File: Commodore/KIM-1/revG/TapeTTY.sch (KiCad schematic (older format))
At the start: 45 parts, among them Q7 Q_NPN_CEB, U15 7400, U16 7404, U26 7438, U27 LM565, U28 LM311, U302 7438

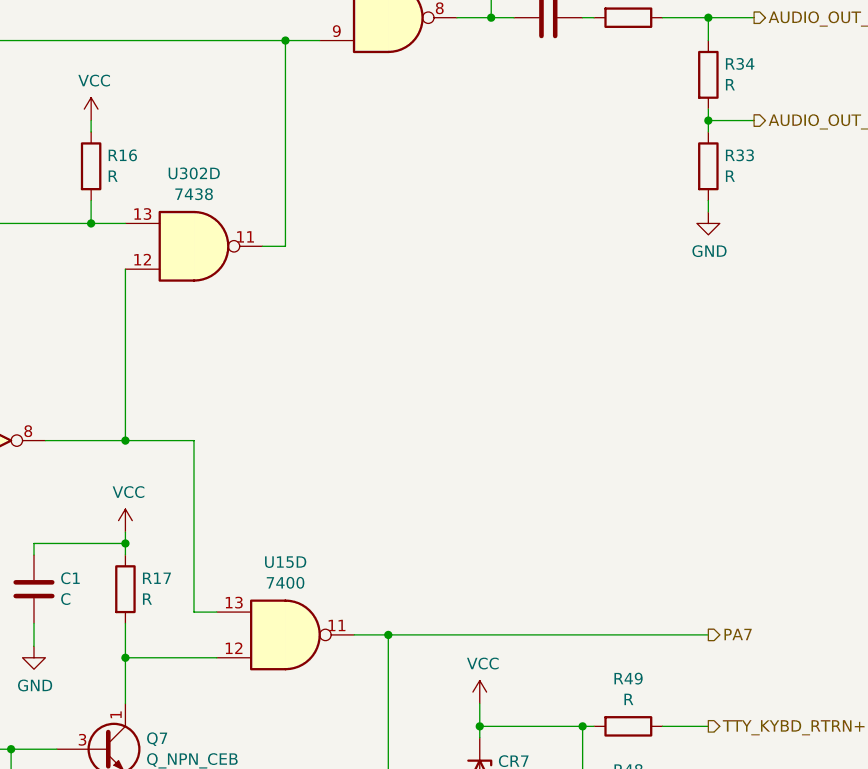
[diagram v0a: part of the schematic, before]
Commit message: Fixed missing/wrong designators, keypad labeling between sheets, PA & PB routing between sheets.
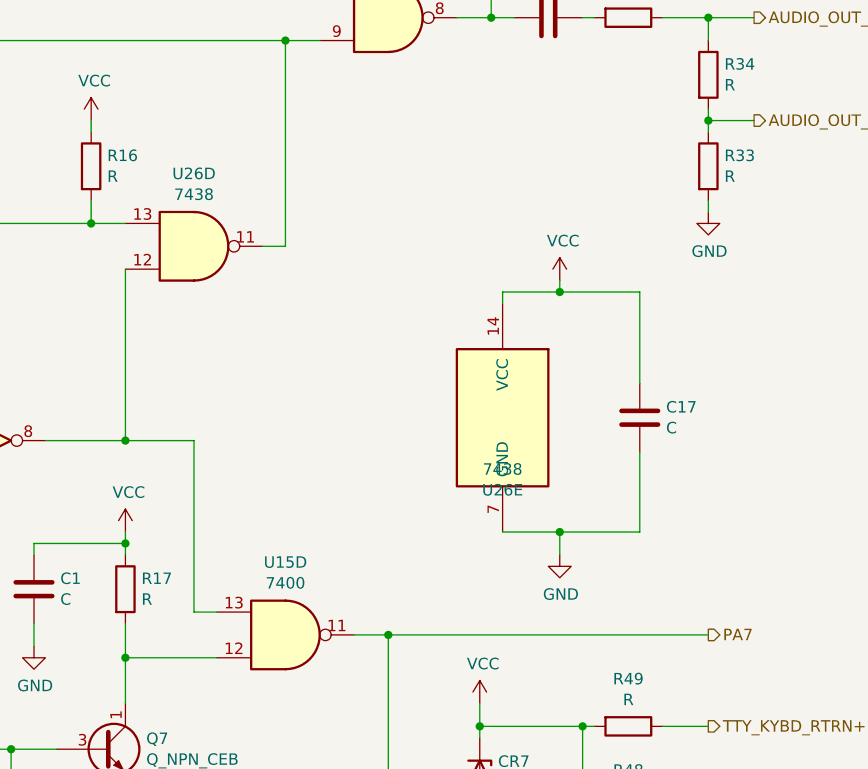
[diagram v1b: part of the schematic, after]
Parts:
- added C17: C, symbol Device:C
- added unit 5 of U26
- renumbered U302 to U26
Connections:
- net GND: now also C17.2, U26.7 (GND)
- net VCC: now also C17.1, U26.14 (VCC)
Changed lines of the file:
@@
 Connection ~ 9400 1500
 $Comp
-L 74xx_more:7438 U302
+L 74xx_more:7438 U26
 U 4 1 62491270
 P 8100 2500
-F 0 "U302" H 8100 2183 50  0000 C CNN
+F 0 "U26" H 8100 2183 50  0000 C CNN
 F 1 "7438" H 8100 2274 50  0000 C CNN
 F 2 "" H 8100 2500 50  0001 C CNN
@@
 Wire Wire Line
 	4500 4500 4500 4150
+$Comp
+L 74xx_more:7438 U26
+U 5 1 60E8022F
+P 9450 3250
+F 0 "U26" H 9450 2933 50  0000 C CNN
+F 1 "7438" H 9450 3024 50  0000 C CNN
+F 2 "" H 9450 3250 50  0001 C CNN
+F 3 "http://www.ti.com/lit/gpn/sn7438" H 9450 3250 50  0001 C CNN
+	5    9450 3250
+	-1   0    0    -1
+$EndComp
+$Comp
+L power:VCC #PWR0162
+U 1 1 60E94919
+P 9700 2650
+F 0 "#PWR0162" H 9700 2500 50  0001 C CNN
+F 1 "VCC" H 9715 2823 50  0000 C CNN
+F 2 "" H 9700 2650 50  0001 C CNN
+F 3 "" H 9700 2650 50  0001 C CNN
+	1    9700 2650
+	1    0    0    -1
+$EndComp
+$Comp
+L power:GND #PWR0163
+U 1 1 60E9528A
+P 9700 3850
+F 0 "#PWR0163" H 9700 3600 50  0001 C CNN
+F 1 "GND" H 9705 3677 50  0000 C CNN
+F 2 "" H 9700 3850 50  0001 C CNN
+F 3 "" H 9700 3850 50  0001 C CNN
+	1    9700 3850
+	1    0    0    -1
+$EndComp
+$Comp
+L Device:C C17
+U 1 1 60E959A3
+P 10050 3250
+F 0 "C17" H 10165 3296 50  0000 L CNN
+F 1 "C" H 10165 3205 50  0000 L CNN
+F 2 "" H 10088 3100 50  0001 C CNN
+F 3 "~" H 10050 3250 50  0001 C CNN
+	1    10050 3250
+	1    0    0    -1
+$EndComp
+Wire Wire Line
+	9450 2750 9450 2700
+Wire Wire Line
+	9450 2700 9700 2700
+Wire Wire Line
+	9700 2700 9700 2650
+Wire Wire Line
+	10050 3100 10050 2700
+Wire Wire Line
+	10050 2700 9700 2700
+Connection ~ 9700 2700
+Wire Wire Line
+	9450 3750 9700 3750
+Wire Wire Line
+	9700 3750 9700 3850
+Wire Wire Line
+	9700 3750 10050 3750
+Wire Wire Line
+	10050 3750 10050 3400
+Connection ~ 9700 3750
 $EndSCHEMATC

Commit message: Updated component values.
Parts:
- C1, C4: value C -> 1uF
- C10, C11, C9: value C -> 0.0068uF
- C12: value C -> 0.047uF
- C13: value C -> 0.022uF
- C14: value C -> 0.001uF
- C17, C7, C8: value C -> 0.1uF
- C5: value C -> 0.33uF
- C6: value C -> 0.22uF
- CR1, CR2, CR3, CR4: value D -> 1N914
- CR5, CR6: value D -> 1N4001
- CR7: value D_Zener -> 1N4735
- Q7: value Q_NPN_CEB -> 2N5371
- R10, R11, R8, R9: value R -> 10K
- R14, R15, R16, R17: value R -> 1K
- R33: value R -> 47
- R34, R50: value R -> 2.2K
- R40: value R -> 560
- R47: value R -> 220
- R48, R49: value R -> 150
- R51: value R -> 30K
- R52: value R -> 5M
- R6: value R -> 3.3K
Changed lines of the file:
@@
 P 10000 5000
 F 0 "R48" V 9793 5000 50  0000 C CNN
-F 1 "R" V 9884 5000 50  0000 C CNN
+F 1 "150" V 9884 5000 50  0000 C CNN
 F 2 "" V 9930 5000 50  0001 C CNN
 F 3 "~" H 10000 5000 50  0001 C CNN
@@
 P 7400 4000
 F 0 "C1" H 7515 4046 50  0000 L CNN
-F 1 "C" H 7515 3955 50  0000 L CNN
+F 1 "1uF" H 7515 3955 50  0000 L CNN
 F 2 "" H 7438 3850 50  0001 C CNN
 F 3 "~" H 7400 4000 50  0001 C CNN
@@
 P 9850 6000
 F 0 "CR6" V 9804 6080 50  0000 L CNN
-F 1 "D" V 9895 6080 50  0000 L CNN
+F 1 "1N4001" V 9895 6080 50  0000 L CNN
 F 2 "" H 9850 6000 50  0001 C CNN
 F 3 "~" H 9850 6000 50  0001 C CNN
@@
 P 9350 4800
 F 0 "CR7" V 9304 4880 50  0000 L CNN
-F 1 "D_Zener" V 9395 4880 50  0000 L CNN
+F 1 "1N4735" V 9395 4880 50  0000 L CNN
 F 2 "" H 9350 4800 50  0001 C CNN
 F 3 "~" H 9350 4800 50  0001 C CNN
@@
 P 7700 4700
 F 0 "Q7" H 7891 4746 50  0000 L CNN
-F 1 "Q_NPN_CEB" H 7891 4655 50  0000 L CNN
+F 1 "2N5371" H 7891 4655 50  0000 L CNN
 F 2 "" H 7900 4800 50  0001 C CNN
 F 3 "~" H 7700 4700 50  0001 C CNN
@@
 P 7800 4000
 F 0 "R17" H 7870 4046 50  0000 L CNN
-F 1 "R" H 7870 3955 50  0000 L CNN
+F 1 "1K" H 7870 3955 50  0000 L CNN
 F 2 "" V 7730 4000 50  0001 C CNN
 F 3 "~" H 7800 4000 50  0001 C CNN
@@
 P 7300 5000
 F 0 "R47" H 7370 5046 50  0000 L CNN
-F 1 "R" H 7370 4955 50  0000 L CNN
+F 1 "220" H 7370 4955 50  0000 L CNN
 F 2 "" V 7230 5000 50  0001 C CNN
 F 3 "~" H 7300 5000 50  0001 C CNN
@@
 P 6900 5000
 F 0 "C5" H 7015 5046 50  0000 L CNN
-F 1 "C" H 7015 4955 50  0000 L CNN
+F 1 "0.33uF" H 7015 4955 50  0000 L CNN
 F 2 "" H 6938 4850 50  0001 C CNN
 F 3 "~" H 6900 5000 50  0001 C CNN
@@
 P 6400 5000
 F 0 "CR5" V 6354 5080 50  0000 L CNN
-F 1 "D" V 6445 5080 50  0000 L CNN
+F 1 "1N4001" V 6445 5080 50  0000 L CNN
 F 2 "" H 6400 5000 50  0001 C CNN
 F 3 "~" H 6400 5000 50  0001 C CNN
@@
 P 10000 4600
 F 0 "R49" V 9793 4600 50  0000 C CNN
-F 1 "R" V 9884 4600 50  0000 C CNN
+F 1 "150" V 9884 4600 50  0000 C CNN
 F 2 "" V 9930 4600 50  0001 C CNN
 F 3 "~" H 10000 4600 50  0001 C CNN
@@
 P 10350 1750
 F 0 "R34" H 10420 1796 50  0000 L CNN
-F 1 "R" H 10420 1705 50  0000 L CNN
+F 1 "2.2K" H 10420 1705 50  0000 L CNN
 F 2 "" V 10280 1750 50  0001 C CNN
 F 3 "~" H 10350 1750 50  0001 C CNN
@@
 P 10350 2150
 F 0 "R33" H 10420 2196 50  0000 L CNN
-F 1 "R" H 10420 2105 50  0000 L CNN
+F 1 "47" H 10420 2105 50  0000 L CNN
 F 2 "" V 10280 2150 50  0001 C CNN
 F 3 "~" H 10350 2150 50  0001 C CNN
@@
 P 10000 1500
 F 0 "R6" V 9793 1500 50  0000 C CNN
-F 1 "R" V 9884 1500 50  0000 C CNN
+F 1 "3.3K" V 9884 1500 50  0000 C CNN
 F 2 "" V 9930 1500 50  0001 C CNN
 F 3 "~" H 10000 1500 50  0001 C CNN
@@
 P 9650 1500
 F 0 "C4" V 9398 1500 50  0000 C CNN
-F 1 "C" V 9489 1500 50  0000 C CNN
+F 1 "1uF" V 9489 1500 50  0000 C CNN
 F 2 "" H 9688 1350 50  0001 C CNN
 F 3 "~" H 9650 1500 50  0001 C CNN
@@
 P 9400 1150
 F 0 "R40" H 9470 1196 50  0000 L CNN
-F 1 "R" H 9470 1105 50  0000 L CNN
+F 1 "560" H 9470 1105 50  0000 L CNN
 F 2 "" V 9330 1150 50  0001 C CNN
 F 3 "~" H 9400 1150 50  0001 C CNN
@@
 P 7650 2150
 F 0 "R16" H 7720 2196 50  0000 L CNN
-F 1 "R" H 7720 2105 50  0000 L CNN
+F 1 "1K" H 7720 2105 50  0000 L CNN
 F 2 "" V 7580 2150 50  0001 C CNN
 F 3 "~" H 7650 2150 50  0001 C CNN
@@
 P 4900 1800
 F 0 "R52" V 4693 1800 50  0000 C CNN
-F 1 "R" V 4784 1800 50  0000 C CNN
+F 1 "5M" V 4784 1800 50  0000 C CNN
 F 2 "" V 4830 1800 50  0001 C CNN
 F 3 "~" H 4900 1800 50  0001 C CNN
@@
 P 4000 2250
 F 0 "C11" H 4115 2296 50  0000 L CNN
-F 1 "C" H 4115 2205 50  0000 L CNN
+F 1 "0.0068uF" H 4115 2205 50  0000 L CNN
 F 2 "" H 4038 2100 50  0001 C CNN
 F 3 "~" H 4000 2250 50  0001 C CNN
@@
 U 1 1 6253C63B
 P 3500 2500
-F 0 "R11" V 3293 2500 50  0000 C CNN
-F 1 "R" V 3384 2500 50  0000 C CNN
+F 0 "R11" V 3700 2500 50  0000 C CNN
+F 1 "10K" V 3600 2500 50  0000 C CNN
 F 2 "" V 3430 2500 50  0001 C CNN
 F 3 "~" H 3500 2500 50  0001 C CNN
@@
 P 3150 2250
 F 0 "C10" H 3265 2296 50  0000 L CNN
-F 1 "C" H 3265 2205 50  0000 L CNN
+F 1 "0.0068uF" H 3265 2205 50  0000 L CNN
 F 2 "" H 3188 2100 50  0001 C CNN
 F 3 "~" H 3150 2250 50  0001 C CNN
@@
 U 1 1 6253D3D7
 P 2800 2500
-F 0 "R10" V 2593 2500 50  0000 C CNN
-F 1 "R" V 2684 2500 50  0000 C CNN
+F 0 "R10" V 3000 2500 50  0000 C CNN
+F 1 "10K" V 2900 2500 50  0000 C CNN
 F 2 "" V 2730 2500 50  0001 C CNN
 F 3 "~" H 2800 2500 50  0001 C CNN
@@
 P 2450 2250
 F 0 "C9" H 2565 2296 50  0000 L CNN
-F 1 "C" H 2565 2205 50  0000 L CNN
+F 1 "0.0068uF" H 2565 2205 50  0000 L CNN
 F 2 "" H 2488 2100 50  0001 C CNN
 F 3 "~" H 2450 2250 50  0001 C CNN
@@
 U 1 1 625467C7
 P 2100 2500
-F 0 "R9" V 1893 2500 50  0000 C CNN
-F 1 "R" V 1984 2500 50  0000 C CNN
+F 0 "R9" V 2300 2500 50  0000 C CNN
+F 1 "10K" V 2200 2500 50  0000 C CNN
 F 2 "" V 2030 2500 50  0001 C CNN
 F 3 "~" H 2100 2500 50  0001 C CNN
@@
 P 1750 2250
 F 0 "C12" H 1865 2296 50  0000 L CNN
-F 1 "C" H 1865 2205 50  0000 L CNN
+F 1 "0.047uF" H 1865 2205 50  0000 L CNN
 F 2 "" H 1788 2100 50  0001 C CNN
 F 3 "~" H 1750 2250 50  0001 C CNN
@@
 P 1300 2250
 F 0 "C8" H 1415 2296 50  0000 L CNN
-F 1 "C" H 1415 2205 50  0000 L CNN
+F 1 "0.1uF" H 1415 2205 50  0000 L CNN
 F 2 "" H 1338 2100 50  0001 C CNN
 F 3 "~" H 1300 2250 50  0001 C CNN
@@
 P 1450 5350
 F 0 "C6" V 1198 5350 50  0000 C CNN
-F 1 "C" V 1289 5350 50  0000 C CNN
+F 1 "0.22uF" V 1289 5350 50  0000 C CNN
 F 2 "" H 1488 5200 50  0001 C CNN
 F 3 "~" H 1450 5350 50  0001 C CNN
@@
 P 2600 5000
 F 0 "CR1" V 2554 5080 50  0000 L CNN
-F 1 "D" V 2645 5080 50  0000 L CNN
+F 1 "1N914" V 2645 5080 50  0000 L CNN
 F 2 "" H 2600 5000 50  0001 C CNN
 F 3 "~" H 2600 5000 50  0001 C CNN
@@
 P 2950 5000
 F 0 "CR2" V 2996 4920 50  0000 R CNN
-F 1 "D" V 2905 4920 50  0000 R CNN
+F 1 "1N914" V 2905 4920 50  0000 R CNN
 F 2 "" H 2950 5000 50  0001 C CNN
 F 3 "~" H 2950 5000 50  0001 C CNN
@@
 P 3300 5000
 F 0 "R15" H 3230 4954 50  0000 R CNN
-F 1 "R" H 3230 5045 50  0000 R CNN
+F 1 "1K" H 3230 5045 50  0000 R CNN
 F 2 "" V 3230 5000 50  0001 C CNN
 F 3 "~" H 3300 5000 50  0001 C CNN
@@
 P 2000 5350
 F 0 "R8" V 1793 5350 50  0000 C CNN
-F 1 "R" V 1884 5350 50  0000 C CNN
+F 1 "10K" V 1884 5350 50  0000 C CNN
 F 2 "" V 1930 5350 50  0001 C CNN
 F 3 "~" H 2000 5350 50  0001 C CNN
@@
 P 2200 5000
 F 0 "R14" H 2130 4954 50  0000 R CNN
-F 1 "R" H 2130 5045 50  0000 R CNN
+F 1 "1K" H 2130 5045 50  0000 R CNN
 F 2 "" V 2130 5000 50  0001 C CNN
 F 3 "~" H 2200 5000 50  0001 C CNN
@@
 P 2150 5750
 F 0 "C14" V 2400 5750 50  0000 C CNN
-F 1 "C" V 2300 5750 50  0000 C CNN
+F 1 "0.001uF" V 2300 5750 50  0000 C CNN
 F 2 "" H 2188 5600 50  0001 C CNN
 F 3 "~" H 2150 5750 50  0001 C CNN
@@
 P 3650 4350
 F 0 "R50" H 3580 4304 50  0000 R CNN
-F 1 "R" H 3580 4395 50  0000 R CNN
+F 1 "2.2K" H 3580 4395 50  0000 R CNN
 F 2 "" V 3580 4350 50  0001 C CNN
 F 3 "~" H 3650 4350 50  0001 C CNN
@@
 P 4050 3900
 F 0 "CR3" V 4096 3820 50  0000 R CNN
-F 1 "D" V 4005 3820 50  0000 R CNN
+F 1 "1N914" V 4005 3820 50  0000 R CNN
 F 2 "" H 4050 3900 50  0001 C CNN
 F 3 "~" H 4050 3900 50  0001 C CNN
@@
 P 4050 3500
 F 0 "CR4" V 4096 3420 50  0000 R CNN
-F 1 "D" V 4005 3420 50  0000 R CNN
+F 1 "1N914" V 4005 3420 50  0000 R CNN
 F 2 "" H 4050 3500 50  0001 C CNN
 F 3 "~" H 4050 3500 50  0001 C CNN
@@
 P 3650 3700
 F 0 "C7" H 3535 3654 50  0000 R CNN
-F 1 "C" H 3535 3745 50  0000 R CNN
+F 1 "0.1uF" H 3535 3745 50  0000 R CNN
 F 2 "" H 3688 3550 50  0001 C CNN
 F 3 "~" H 3650 3700 50  0001 C CNN
@@
 P 4850 3900
 F 0 "R51" V 5057 3900 50  0000 C CNN
-F 1 "R" V 4966 3900 50  0000 C CNN
+F 1 "30K" V 4966 3900 50  0000 C CNN
 F 2 "" V 4780 3900 50  0001 C CNN
 F 3 "~" H 4850 3900 50  0001 C CNN
@@
 P 3750 6100
 F 0 "C13" H 3865 6146 50  0000 L CNN
-F 1 "C" H 3865 6055 50  0000 L CNN
+F 1 "0.022uF" H 3865 6055 50  0000 L CNN
 F 2 "" H 3788 5950 50  0001 C CNN
 F 3 "~" H 3750 6100 50  0001 C CNN
@@
 P 10050 3250
 F 0 "C17" H 10165 3296 50  0000 L CNN
-F 1 "C" H 10165 3205 50  0000 L CNN
+F 1 "0.1uF" H 10165 3205 50  0000 L CNN
 F 2 "" H 10088 3100 50  0001 C CNN
 F 3 "~" H 10050 3250 50  0001 C CNN

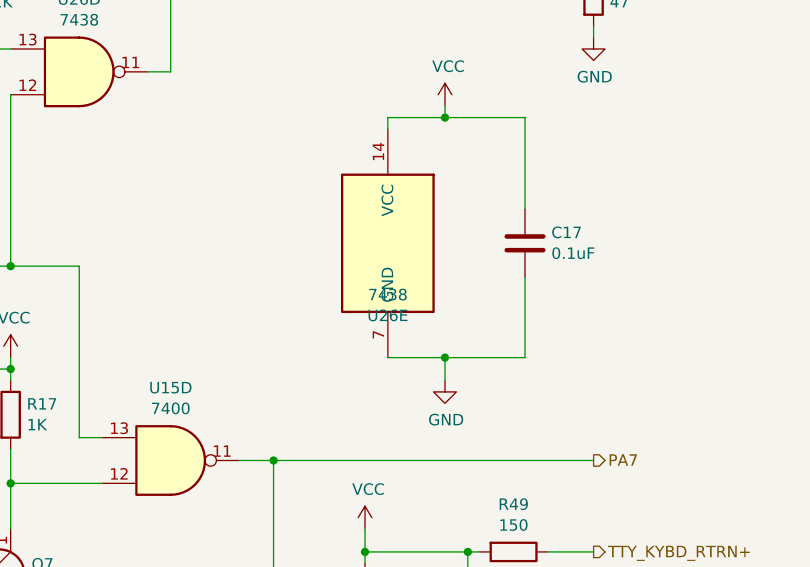
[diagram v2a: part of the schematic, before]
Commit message: Move KIM specific components out of shared libraries into the project library
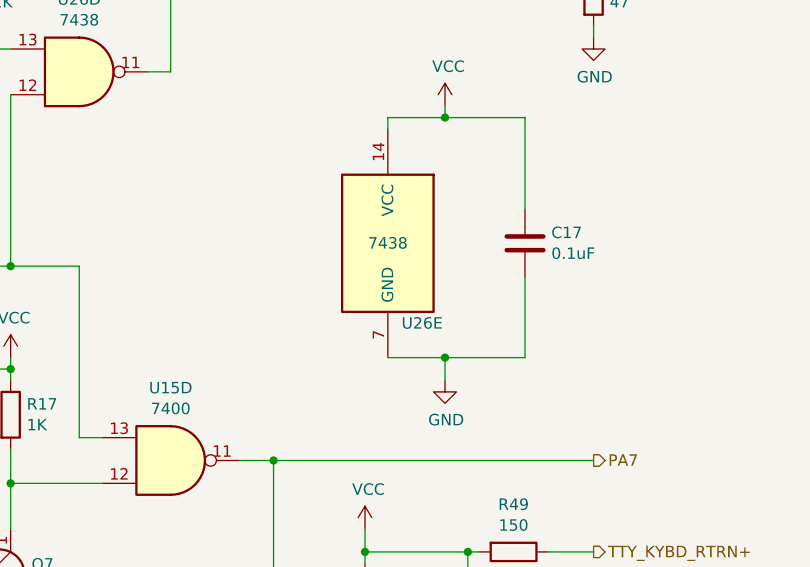
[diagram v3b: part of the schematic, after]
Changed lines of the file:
@@
 U 5 1 60E8022F
 P 9450 3250
-F 0 "U26" H 9450 2933 50  0000 C CNN
-F 1 "7438" H 9450 3024 50  0000 C CNN
+F 0 "U26" H 9300 2900 50  0000 C CNN
+F 1 "7438" H 9450 3250 50  0000 C CNN
 F 2 "" H 9450 3250 50  0001 C CNN
 F 3 "http://www.ti.com/lit/gpn/sn7438" H 9450 3250 50  0001 C CNN
